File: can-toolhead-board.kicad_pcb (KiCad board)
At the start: 4 copper layers, 51 x 36.9 mm, 98 parts, among them J1 MF3-2x2P, J10 PH-2P, J11 PH-2P, J12 PH-2P, J13 PH-2P, J14 PH-2P, J15 PH-3P, J2 USB_C_Receptacle_USB2.0, J3 SH-6P, J4 PH-2P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

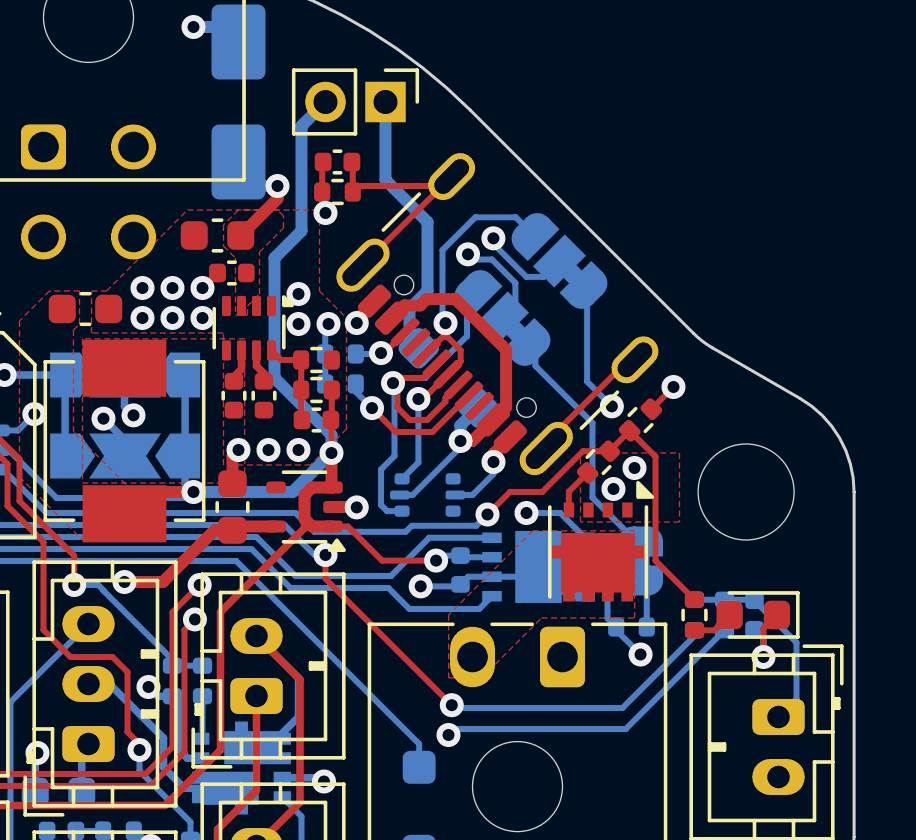
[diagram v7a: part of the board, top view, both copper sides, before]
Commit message: Change 10uF cap on 24V input to 0805; change 33nF to 22nF to simplify BOM; add green power LED
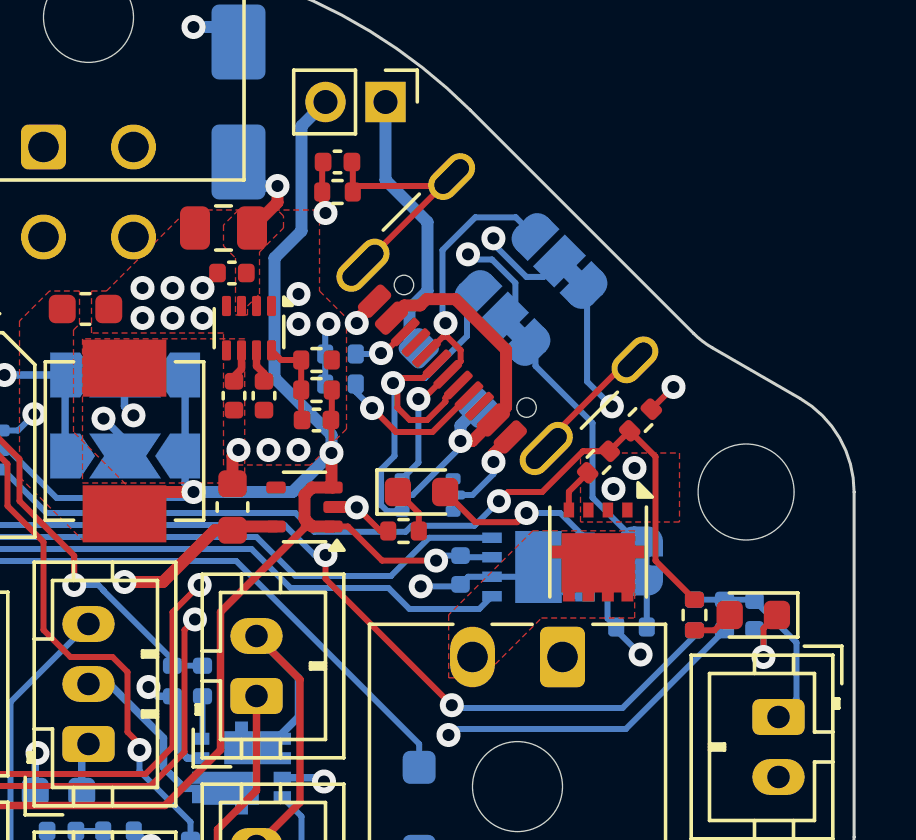
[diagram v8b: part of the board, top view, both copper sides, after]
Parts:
- added D6: Green, LED_SMD:LED_0603_1608Metric, F.Cu at (111.1, 100.0)
- added R31: 10K, Resistor_SMD:R_0402_1005Metric, F.Cu at (110.5, 101.3)
- C2: footprint Capacitor_SMD:C_0603_1608Metric -> Capacitor_SMD:C_0805_2012Metric
- C4: value 33n -> 22n
- moved C2 0.32 mm to (104.5, 91.2)
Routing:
- net +3V3: track 30.6 -> 33.9 mm
- net Net-(D6-K): track 0.00 -> 1.59 mm
- net GND: track 69.1 -> 70.5 mm
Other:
- board text added: "CTB ${PCB_VERSION}"
- board text removed: "CTB v1.0-9999999"
